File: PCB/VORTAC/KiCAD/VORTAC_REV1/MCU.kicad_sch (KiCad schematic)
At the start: 47 parts, among them IC1 TMC2209-LA, SW1 Boot, SW2 Reset, U2 STM32F103C8T6, U8 TJA1044GTK/3Z

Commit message: Gschenkle
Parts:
- removed C44: 10nF, Capacitor_SMD:C_0402_1005Metric, symbol Device:C_Small
- removed C45: 1uF, Capacitor_SMD:C_0402_1005Metric, symbol Device:C_Small
- removed L3: 10uH 15mA, Inductor_SMD:L_0805_2012Metric, symbol Device:L_Small
- removed R33: 10K, Resistor_SMD:R_0402_1005Metric, symbol Device:R_Small
- added R13: 1K, Resistor_SMD:R_0402_1005Metric, symbol Device:R_Small
- R9: value 100R -> 10K
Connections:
- net +3V3: now also R9.2
- net AS_MISO: now also U2.27 (PB14); no longer U2.16 (PA6)
- net AS_MOSI: now also U2.28 (PB15); no longer U2.17 (PA7)
- net ENDSTOP_X: no longer U2.11 (PA1)
- net ENDSTOP_Z: no longer U2.10 (PA0)
- net NRST: now also R9.1
- net TMC_DIAG: now also U2.18 (PB0); no longer R9.2
- net TMC_DIR: now also U2.11 (PA1); no longer U2.29 (PA8)
- net TMC_ENN: now also U2.10 (PA0)
- net TMC_STEP: now also U2.13 (PA3); no longer U2.28 (PB15)
- net TMC_UART: now also R13.2; no longer U2.30 (PA9)
- net TOOL_ID_PIN: no longer U2.41 (PB5)
- net at U2.12 (PA2): now also R13.1
- net AS_NSS: now reaches U2.25 (PB12)
- net AS_SCK: now reaches U2.26 (PB13)
- net at U2.38 (PA15): no longer R9.1
- net AS_CLK: no longer names the net of U2.15 (PA5)
- net AS_NCS: no longer names the net of U2.14 (PA4)
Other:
- note added: "BOOT 0 jumper could be part of debug header"
- note added: "SPI 1"
- note added: "SPI 2"
- note added: "UART 1"
- note added: "UART 2"
- note removed: "Inline Resistor USB??"
- note removed: "Optional Asynchronous SW??"
- note removed: "Removed Analog Refference Voltage Filter"
- note removed: "add ambient sensor on pcb"
- moved on the sheet: C42, C43, HSE1

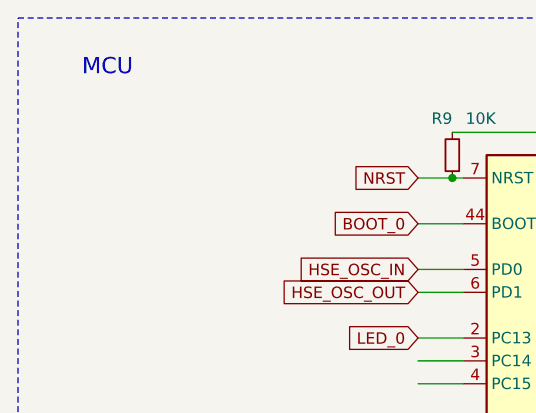
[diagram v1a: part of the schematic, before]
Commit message: Schematic Updates - Changed the 5V Rail to a more space efficient implementation
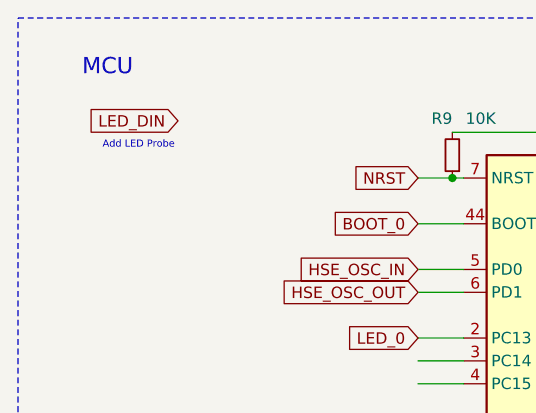
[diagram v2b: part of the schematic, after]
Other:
- note added: "Add LED Probe"
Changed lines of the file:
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@@
+		)
+	)
+	(text "Add LED Probe"
+		(exclude_from_sim no)
+		(at 25.908 30.226 0)
+		(effects
+			(font
+				(size 0.7874 0.7874)
+				(color 255 0 244 1)
+			)
+			(justify left top)
 		)
 	)
@@
 				(hide yes)
 			)
+		)
+	)
+	(global_label "LED_DIN"
+		(shape input)
+		(at 34.29 27.94 180)
+		(fields_autoplaced yes)
+		(effects
+			(font
+				(size 1.27 1.27)
+			)
+			(justify right)
+		)
+		(property "Intersheetrefs" "${INTERSHEET_REFS}"
+			(at 24.339 27.94 0)
+			(effects
+				(font
+					(size 1.27 1.27)
+				)
+				(justify right)
+				(hide yes)
+			)

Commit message: Schematic Updates Madrilla
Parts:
- added R7: 100R, Resistor_SMD:R_0402_1005Metric, symbol Device:R_Small
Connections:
- net ENDSTOP_X: now also U2.17 (PA7)
- net ENDSTOP_Z: now also U2.16 (PA6)
- net LED_DIN: now also R7.1
- net at U2.14 (PA4): now also R7.2
- no-connect marks 2 -> 16
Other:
- note removed: "Add LED Probe"
- note removed: "SPI 1"
- note removed: "SPI 2"
- note removed: "UART 1"
- note removed: "UART 2"
- note removed: "todo -consider AREF implementation -3.3v vs AREF for ADXL & CAN >> routing for can therm and can gets kinda awkward >> can and therm should be unified to AREF or 3.3"
- moved on the sheet: R13, R35, R36, R9, U2

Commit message: pushy
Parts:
- removed JP1: Jumper, Connector_PinHeader_1.27mm:PinHeader_2x01_P1.27mm_Vertical, symbol Jumper:Jumper_2_Small_Open
- added JP2: Jumper, Connector_PinHeader_1.27mm:PinHeader_2x01_P1.27mm_Vertical, symbol Jumper:Jumper_2_Small_Bridged
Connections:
- net CAN_L: now also JP2.2 (B)
- net at R10.2: now also JP2.1 (A)
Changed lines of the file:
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@@
 		)
 	)
-	(global_label "TOOL_ID_PIN"
-		(shape input)
-		(at 101.6 43.18 0)
-		(effects
-			(font
-				(size 1.27 1.27)
-			)
-			(justify left)
-		)
-		(property "Intersheetrefs" "${INTERSHEET_REFS}"
-			(at 101.6 43.18 0)
-			(effects
-				(font
-					(size 1.27 1.27)
-				)
-				(hide yes)
-			)
-		)
-	)
 	(global_label "CAN_H"
 		(shape input)
@@
 	)
 	(symbol
-		(lib_id "VORTAC-rescue:+3.3V-power")
-		(at 127 160.02 270)
+		(lib_id "Jumper:Jumper_2_Small_Bridged")
+		(at 241.3 146.05 90)
 		(unit 1)
 		(exclude_from_sim no)
@@
 		(on_board yes)
 		(dnp no)
-		(property "Reference" "#PWR015"
-			(at 123.19 160.02 0)
+		(property "Reference" "JP2"
+			(at 236.474 144.272 90)
 			(effects
 				(font
 					(size 1.27 1.27)
 				)
-				(hide yes)
+				(justify right)
 			)
 		)
-		(property "Value" "+3V3"
-			(at 133.35 160.02 90)
+		(property "Value" "Jumper"
+			(at 233.426 146.812 90)
 			(effects
 				(font
 					(size 1.27 1.27)
 				)
+				(justify right)
 			)
 		)
-		(property "Footprint" ""
-			(at 127 160.02 0)
+		(property "Footprint" "Connector_PinHeader_1.27mm:PinHeader_2x01_P1.27mm_Vertical"
+			(at 241.3 146.05 0)
 			(effects
 				(font
@@
 			)
 		)
-		(property "Datasheet" ""
-			(at 127 160.02 0)
+		(property "Datasheet" "~"
+			(at 241.3 146.05 0)
 			(effects
 				(font
@@
 			)
 		)
-		(property "Description" ""
-			(at 127 160.02 0)
+		(property "Description" "Jumper, 2-pole, small symbol, bridged"
+			(at 241.3 146.05 0)
 			(effects
 				(font
@@
 			)
 		)
+		(pin "2"
+		)
 		(pin "1"
 		)
 		(instances
-			(project "VORTAC_REV1"
+			(project ""
 				(path "/ed58d858-d9f9-4504-a982-ccfc7f9efbad/00000000-0000-0000-0000-0000613dc005"
-					(reference "#PWR015")
+					(reference "JP2")
 					(unit 1)
 				)
@@
 	)
 	(symbol
-		(lib_id "Jumper:Jumper_2_Small_Open")
-		(at 241.3 146.05 90)
+		(lib_id "VORTAC-rescue:+3.3V-power")
+		(at 127 160.02 270)
 		(unit 1)
-		(exclude_from_sim yes)
+		(exclude_from_sim no)
 		(in_bom yes)
 		(on_board yes)
 		(dnp no)
-		(property "Reference" "JP1"
-			(at 243.332 147.32 0)
+		(property "Reference" "#PWR015"
+			(at 123.19 160.02 0)
 			(effects
 				(font
 					(size 1.27 1.27)
 				)
-				(justify right)
+				(hide yes)
 			)
 		)
-		(property "Value" "Jumper"
-			(at 243.332 139.954 0)
+		(property "Value" "+3V3"
+			(at 133.35 160.02 90)
 			(effects
 				(font
 					(size 1.27 1.27)
 				)
-				(justify right)
 			)
 		)
-		(property "Footprint" "Connector_PinHeader_1.27mm:PinHeader_2x01_P1.27mm_Vertical"
-			(at 241.3 146.05 0)
+		(property "Footprint" ""
+			(at 127 160.02 0)
 			(effects
 				(font
@@
 			)
 		)
-		(property "Datasheet" "~"
-			(at 241.3 146.05 0)
+		(property "Datasheet" ""
+			(at 127 160.02 0)
 			(effects
 				(font
@@
 			)
 		)
-		(property "Description" "Jumper, 2-pole, small symbol, open"
-			(at 241.3 146.05 0)
+		(property "Description" ""
+			(at 127 160.02 0)
 			(effects
 				(font
@@
 			)
 		)
-		(pin "2"
-		)
 		(pin "1"
 		)
@@
 			(project "VORTAC_REV1"
 				(path "/ed58d858-d9f9-4504-a982-ccfc7f9efbad/00000000-0000-0000-0000-0000613dc005"
-					(reference "JP1")
+					(reference "#PWR015")
 					(unit 1)
 				)

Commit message: Update Symbol Librarys
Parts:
- C34: symbol VORTAC-rescue:CP-Device -> Vortac:CP-Device
- U2: symbol VORTAC-rescue:STM32F103C8Tx-MCU_ST_STM32F1 -> Vortac:STM32F103C8Tx-MCU_ST_STM32F1
- renumbered HSE1 to Y1

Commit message: updated tmc library reference
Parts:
- IC1: symbol ToolChanger:TMC2209-LA -> Vortac:TMC2209-LA
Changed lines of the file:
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@@
 	)
 	(symbol
-		(lib_id "ToolChanger:TMC2209-LA")
+		(lib_id "Vortac:TMC2209-LA")
 		(at 209.55 54.61 0)
 		(unit 1)

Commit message: night night
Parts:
- removed JP2: Jumper, Connector_PinHeader_1.27mm:PinHeader_2x01_P1.27mm_Vertical, symbol Jumper:Jumper_2_Small_Bridged
- R10: value 120R -> 110R
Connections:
- net CAN_H: no longer R10.1
- net CAN_L: now also R10.1
- net CAN_TRM: now reaches U2.42 (PB6)
- net CAN_TRM_L: now reaches R10.2
- no-connect marks 16 -> 15
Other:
- note added: "This uses a 110R resistor to compensate for the internal resistance of the 2 BSS138s"
- moved on the sheet: C17, C35, L1, R10, U8
